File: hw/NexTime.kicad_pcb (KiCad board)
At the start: 4 copper layers, 84.2 x 48.8 mm, 80 parts, among them J101 ER-CON40HB-2, J102 pwr+data, J103 CR2032, SW101 Push button switch, U101 SRV05-4, U102 XTAA5212IRGER, U103 ESP32-S3-WROOM-1-N8R8, U104 OPA4863, U105 LMR51430YDDCR, U106 TPS74633PQWDRBRQ1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

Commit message: Improve connector 3d model and footprint now matches connector drawing
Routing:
- net /BOOT0: track 85.4 -> 87.3 mm, vias 2 -> 1
- net GND: track 65.2 -> 66.4 mm
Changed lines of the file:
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@@
 		(attr smd)
 		(fp_rect
-			(start -3.64 -8.92)
-			(end 42.66 0.08)
+			(start -3.74 -8.92)
+			(end 43.26 0.08)
 			(stroke
 				(width 0.1)
@@
 		)
 		(fp_rect
-			(start -4.13 -8.92)
-			(end 42.89 0.22)
+			(start -3.83 -8.92)
+			(end 43.39 0.22)
 			(stroke
 				(width 0.05)
@@
 		)
 		(pad "40" smd rect
-			(at 41.5 -3.15)
+			(at 42.1 -3.15)
 			(size 2 2.5)
 			(layers "F.Cu" "F.Mask" "F.Paste")
@@
 			(opacity 0.7800)
 			(offset
-				(xyz 19.9 5.5 0)
+				(xyz 19.8 5.5 0)
 			)
 			(scale
@@
 	)
 	(segment
-		(start 111.45 92.35)
-		(end 111.4 92.3)
-		(width 0.2)
-		(layer "F.Cu")
-		(net 1)
-	)
-	(segment
 		(start 71.820063 111.550063)
 		(end 71.050063 111.550063)
@@
 	)
 	(segment
+		(start 68.99 94.09)
+		(end 69 94.1)
+		(width 0.2)
+		(layer "F.Cu")
+		(net 1)
+	)
+	(segment
 		(start 124.23 125)
 		(end 125.275 125)
@@
 	)
 	(segment
+		(start 113.59 92.35)
+		(end 113.59 94.19)
+		(width 0.2)
+		(layer "F.Cu")
+		(net 1)
+	)
+	(segment
 		(start 77.300063 111.257278)
 		(end 77.300063 111.950063)
@@
 	)
 	(segment
-		(start 112.99 92.35)
-		(end 111.45 92.35)
-		(width 0.2)
-		(layer "F.Cu")
-		(net 1)
-	)
-	(segment
 		(start 99.691429 123.494402)
 		(end 99.485831 123.7)
@@
 	)
 	(segment
-		(start 67.4 93.2)
-		(end 68.14 93.2)
-		(width 0.2)
-		(layer "F.Cu")
-		(net 1)
-	)
-	(segment
 		(start 77.826063 114.87612)
 		(end 77.87612 114.87612)
@@
 	)
 	(segment
+		(start 68.99 92.35)
+		(end 68.99 94.09)
+		(width 0.2)
+		(layer "F.Cu")
+		(net 1)
+	)
+	(segment
 		(start 130.6 102.15)
 		(end 129.85 102.9)
@@
 	)
 	(segment
+		(start 113.59 94.19)
+		(end 113.6 94.2)
+		(width 0.2)
+		(layer "F.Cu")
+		(net 1)
+	)
+	(segment
 		(start 77.87612 114.87612)
 		(end 78.300063 115.300063)
@@
 	)
 	(via
-		(at 111.4 92.3)
-		(size 0.6)
-		(drill 0.3)
-		(layers "F.Cu" "B.Cu")
-		(net 1)
-	)
-	(via
 		(at 53.8 122.19)
 		(size 0.6)
@@
 	)
 	(via
+		(at 113.6 94.2)
+		(size 0.6)
+		(drill 0.3)
+		(layers "F.Cu" "B.Cu")
+		(net 1)
+	)
+	(via
 		(at 91 124.285)
 		(size 0.6)
@@
 	)
 	(via
+		(at 69 94.1)
+		(size 0.6)
+		(drill 0.3)
+		(layers "F.Cu" "B.Cu")
+		(net 1)
+	)
+	(via
 		(at 55.6 114.9)
 		(size 0.6)
@@
 	)
 	(via
-		(at 67.4 93.2)
-		(size 0.6)
-		(drill 0.3)
-		(layers "F.Cu" "B.Cu")
-		(net 1)
-	)
-	(via
 		(at 81.2 97.7)
 		(size 0.6)
@@
 	)
 	(segment
+		(start 127.35 98.65)
+		(end 116.6 87.9)
+		(width 0.2)
+		(layer "F.Cu")
+		(net 61)
+	)
+	(segment
 		(start 67.6 98.3)
 		(end 67.6 98.1)
@@
 	)
 	(segment
-		(start 67.6 98.1)
-		(end 67.6 96.59)
+		(start 67.1 97.5)
+		(end 67.6 98)
 		(width 0.2)
 		(layer "F.Cu")
@@
 	)
 	(segment
-		(start 127.35 102.95)
-		(end 128.9 101.4)
+		(start 67.1 89.6)
+		(end 67.1 97.5)
+		(width 0.2)
+		(layer "F.Cu")
+		(net 61)
+	)
+	(segment
+		(start 67.6 98)
+		(end 67.6 98.1)
 		(width 0.2)
 		(layer "F.Cu")
@@
 	)
 	(segment
-		(start 67.6 96.59)
-		(end 71.1 93.09)
+		(start 116.6 87.9)
+		(end 68.8 87.9)
 		(width 0.2)
 		(layer "F.Cu")
@@
 	)
 	(segment
-		(start 71.1 87.9)
-		(end 71.1 93.09)
+		(start 127.35 102.95)
+		(end 128.9 101.4)
 		(width 0.2)
 		(layer "F.Cu")
@@
 	)
 	(segment
+		(start 68.8 87.9)
+		(end 67.1 89.6)
+		(width 0.2)
+		(layer "F.Cu")
+		(net 61)
+	)
+	(segment
 		(start 128.6 106.65)
 		(end 127.35 105.4)
@@
 		(net 61)
 	)
-	(via
-		(at 127.35 102.95)
-		(size 0.6)
-		(drill 0.3)
-		(layers "F.Cu" "B.Cu")
+	(segment
+		(start 127.35 102.95)
+		(end 127.35 98.65)
+		(width 0.2)
+		(layer "F.Cu")
 		(net 61)
 	)
 	(via
-		(at 71.1 87.9)
+		(at 127.35 102.95)
 		(size 0.6)
 		(drill 0.3)
@@
 		(net 61)
 	)
-	(segment
-		(start 116.6 87.9)
-		(end 127.35 98.65)
-		(width 0.2)
-		(layer "B.Cu")
-		(net 61)
-	)
-	(segment
-		(start 71.2 87.9)
-		(end 116.6 87.9)
-		(width 0.2)
-		(layer "B.Cu")
-		(net 61)
-	)
-	(segment
-		(start 127.35 98.65)
-		(end 127.35 102.95)
-		(width 0.2)
-		(layer "B.Cu")
-		(net 61)
-	)

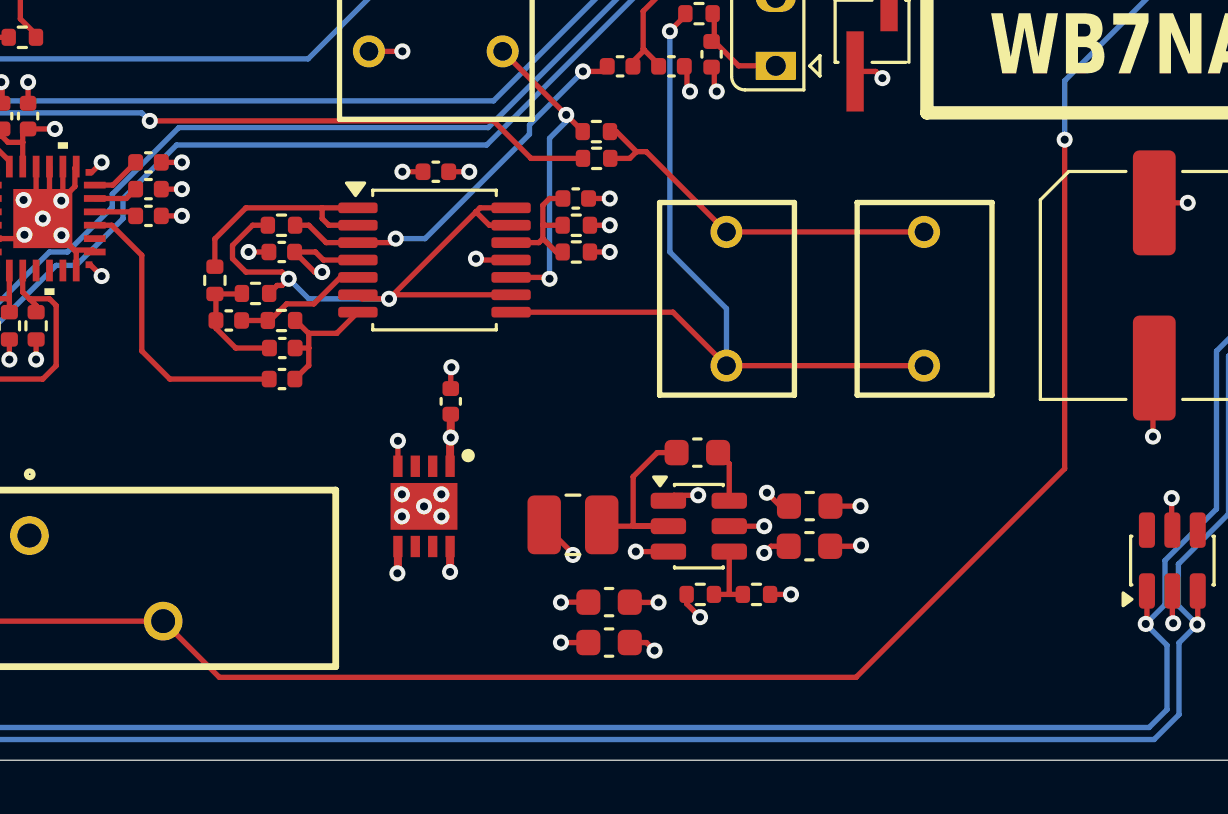
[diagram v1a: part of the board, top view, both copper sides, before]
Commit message: Improve power routing
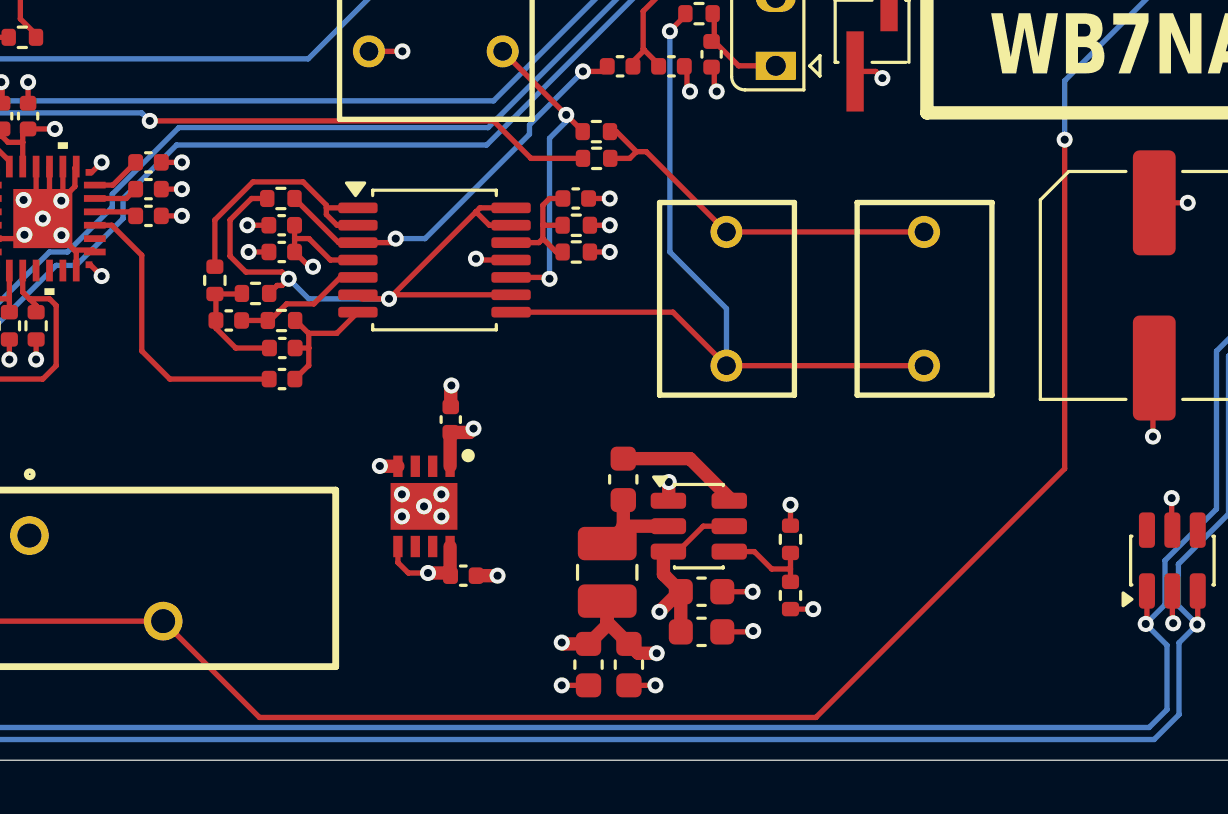
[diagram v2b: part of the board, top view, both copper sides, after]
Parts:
- added C138: 1uF, Capacitor_SMD:C_0402_1005Metric, F.Cu at (91.8, 126.5)
- moved C136 6.10 mm to (85.0, 113.4), turned to 180 degrees
- moved C130 5.16 mm to (100.7, 127.1)
- moved C131 5.15 mm to (100.7, 128.6)
- moved R117 3.37 mm to (104.0, 127.2), turned to -90 degrees
- moved C129 2.94 mm to (97.8, 122.9), turned to -90 degrees
- moved C133 2.46 mm to (96.5, 129.8), turned to -90 degrees
- moved R119 2.42 mm to (104.0, 125.1), turned to -90 degrees
- moved L102 2.19 mm to (97.2, 126.4), turned to -90 degrees
- moved C132 1.11 mm to (98.0, 129.8), turned to -90 degrees
- moved R105 1.00 mm to (85.0, 112.4)
- moved C134 0.68 mm to (91.3, 120.7)
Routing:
- net VBUS: track 12.6 -> 16.9 mm, vias 11 -> 7
- net Net-(U105-SW): track 7.30 -> 3.55 mm
- net Net-(U105-CB): track 1.97 -> 4.67 mm
- net +3.3V: track 26.5 -> 28.6 mm, vias 14 -> 13
- net Net-(Y101-VBACKUP): track 83.8 -> 85.1 mm
- net /vaGND: track 22.9 -> 24.0 mm
- net Net-(U104A--): track 8.71 -> 9.74 mm
- net Net-(U105-FB): track 2.68 -> 3.64 mm
- net +AVDD: track 10.9 -> 11.1 mm, vias 5 -> 4
- net GND: vias 80 -> 81

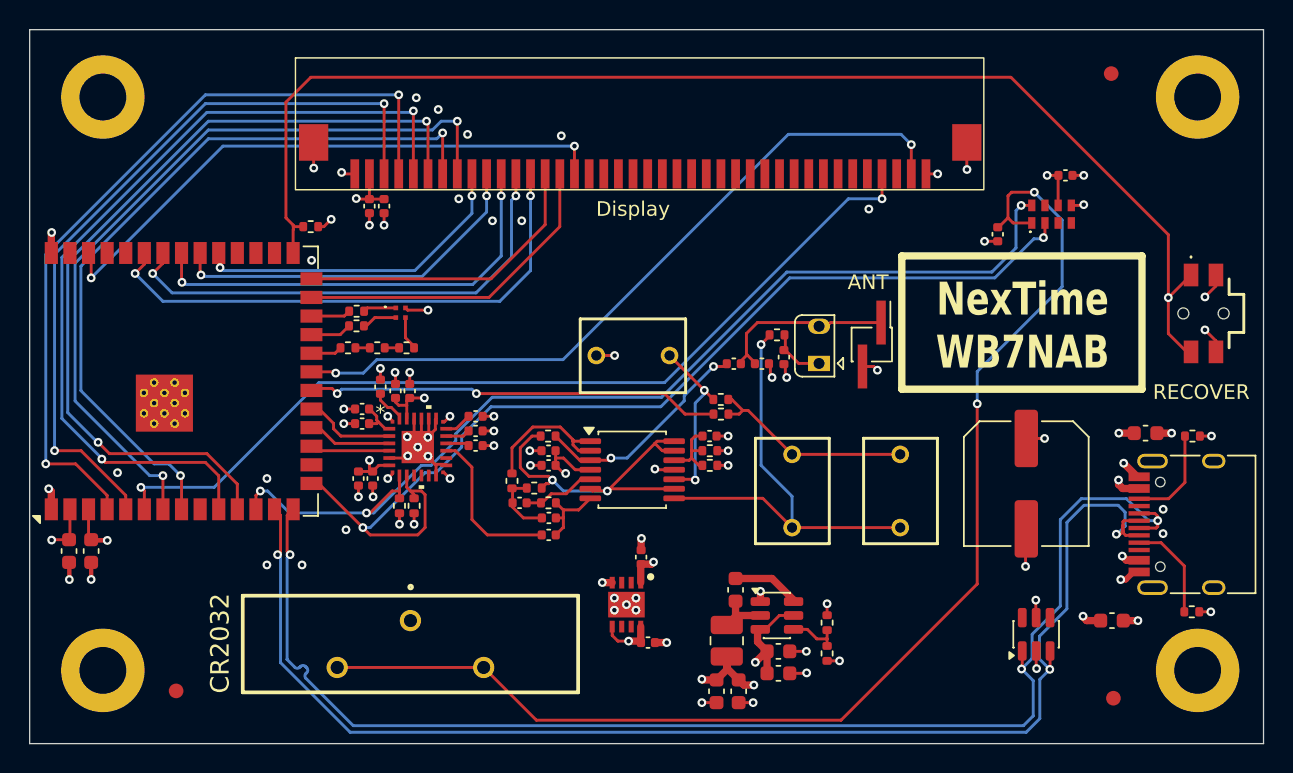
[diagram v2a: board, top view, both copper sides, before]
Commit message: Move things around to make room for FLAT CR2032 bat holder. Add RF shield ring around high Z sensitivity circuitry. Shove display connector toward board left and move RECOVER button up on top by display connector. Move temp sensitive RTC away from heat producing components.
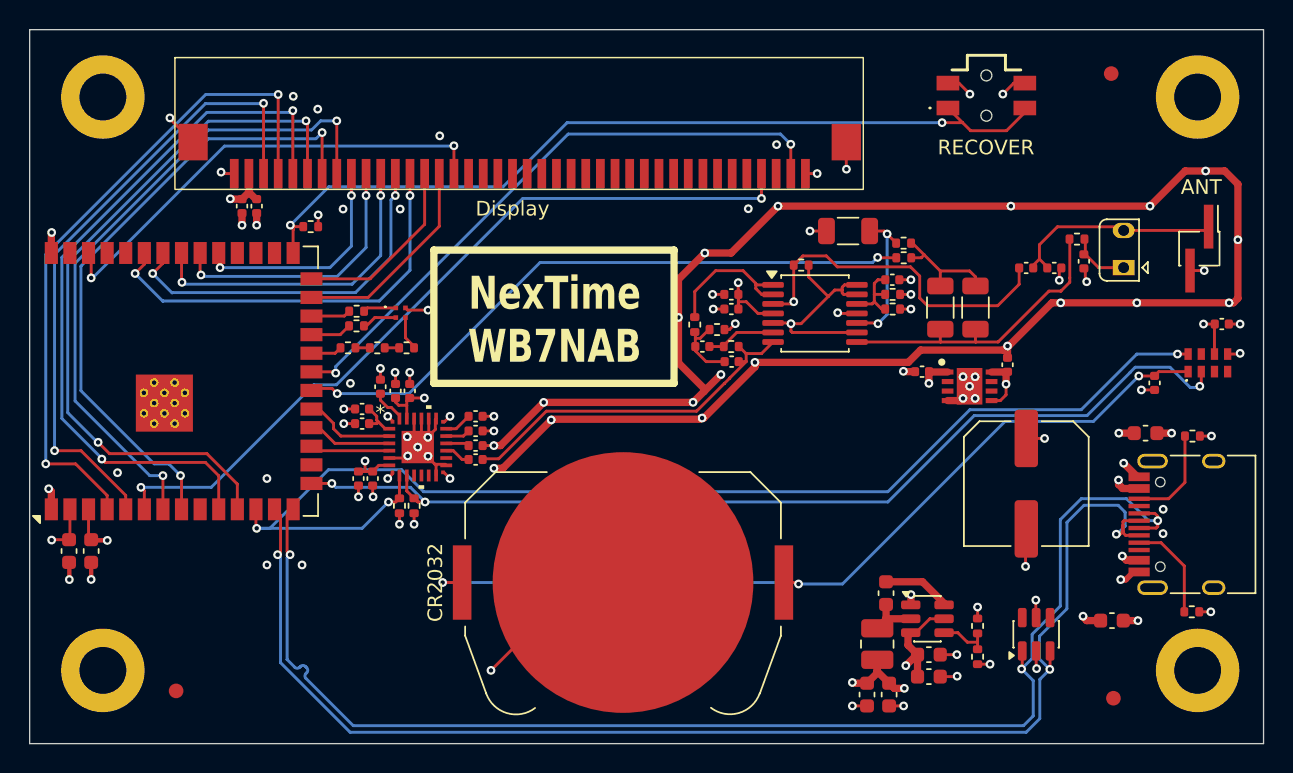
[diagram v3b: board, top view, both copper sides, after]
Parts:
- removed J103: CR2032, Library:S8401-46
- added BT101: CR2032, Battery:BatteryHolder_Keystone_3034_1x20mm, F.Cu at (90.1, 122.4)
- C117, C122: value 1nF -> 1nF NP0
- C118, C119, C125: value 1uF PP -> 100nF NP0; footprint Library:R82DC4100AA60K -> Capacitor_SMD:C_1206_3216Metric
- R106: value 78.7k -> 42.1k
- R108: value 11k -> 110k
- R109: value 20k -> 200k
- R110: value 78.7k -> 21k
- R111: value 88.7k -> 169
- moved C138 31.0 mm to (116.4, 107.5), turned to 90 degrees
- moved U106 27.8 mm to (113.8, 109.0), turned to 0 degrees
- moved L101 23.3 mm to (129.5, 99.6)
- moved C134 23.0 mm to (110.5, 108.0), turned to 180 degrees
- moved D101 21.8 mm to (124.3, 100.9)
- moved C128 21.5 mm to (121.6, 100.5)
- moved R112 21.5 mm to (121.1, 99.0)
- moved C120 21.0 mm to (117.6, 100.9)
- moved C124 21.0 mm to (119.6, 100.9)
- moved SW101 21.0 mm to (114.9, 89.2), turned to 180 degrees
- moved R105 20.9 mm to (102.3, 100.7), turned to 0 degrees
- moved R111 16.5 mm to (96.5, 105.1)
- moved C117 16.4 mm to (97.5, 107.3)
- moved C122 16.4 mm to (95.5, 106.3)
- moved C135 16.4 mm to (97.5, 103.7)
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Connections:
- C122 pad 2: Net-(U104B-+) -> Net-(U104B--)
- R106 pad 1: Net-(U104B-+) -> Net-(U104B--)
- R111 pad 1: /vaGND -> GND
- U104 pad 5: Net-(U104B-+) -> /vaGND
- U104 pad 6: /vaGND -> Net-(U104B--)
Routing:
- net GND: track 66.4 -> 207.1 mm, vias 81 -> 95
- net /BOOT0: track 87.3 -> 57.9 mm, vias 1 -> 2
- net Net-(BT101-+): track 85.1 -> 59.3 mm, vias 2 -> 3
- net Net-(C117-Pad2): track 5.30 -> 24.6 mm
- net /tunePWM: track 28.3 -> 43.8 mm
- net /SCL: track 69.3 -> 83.2 mm
- net Net-(C118-Pad2): track 30.6 -> 20.9 mm, vias 1 -> 0
- net Net-(U102A-IN1P): track 11.0 -> 1.78 mm
- net Net-(U104A-+): track 15.1 -> 23.6 mm, vias 2 -> 1
- net /dispNCS: track 52.0 -> 43.8 mm
- net /dispD7: track 40.1 -> 31.9 mm, vias 2 -> 4
- net /dispD4: track 36.9 -> 28.7 mm
- net /dispD5: track 21.0 -> 12.7 mm
- net /dispD6: track 22.6 -> 14.3 mm
- net /dispD3: track 33.6 -> 25.3 mm
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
